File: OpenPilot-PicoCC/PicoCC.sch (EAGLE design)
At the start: 6 parts, among them U1 STM32F103CBT6, X1 MINI-USB-SCHIELD-32005-301

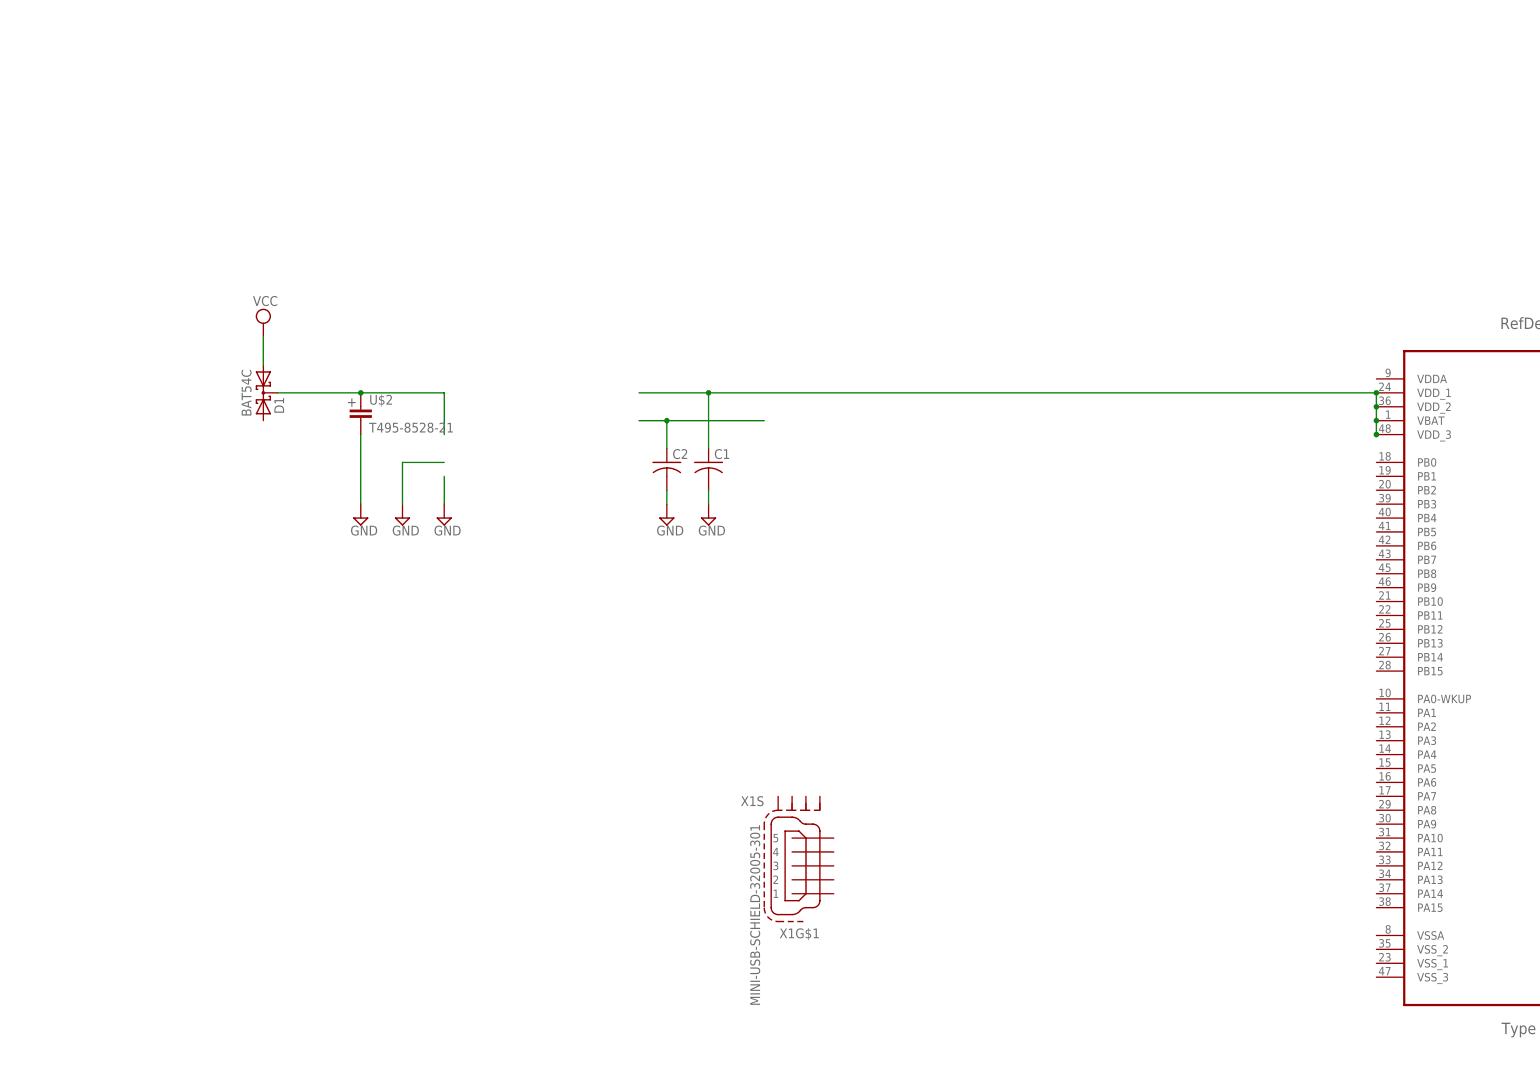
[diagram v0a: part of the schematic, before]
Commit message: Adding a Few things as we go, nice new line protection on the "servo" connectors to prevent shorts.
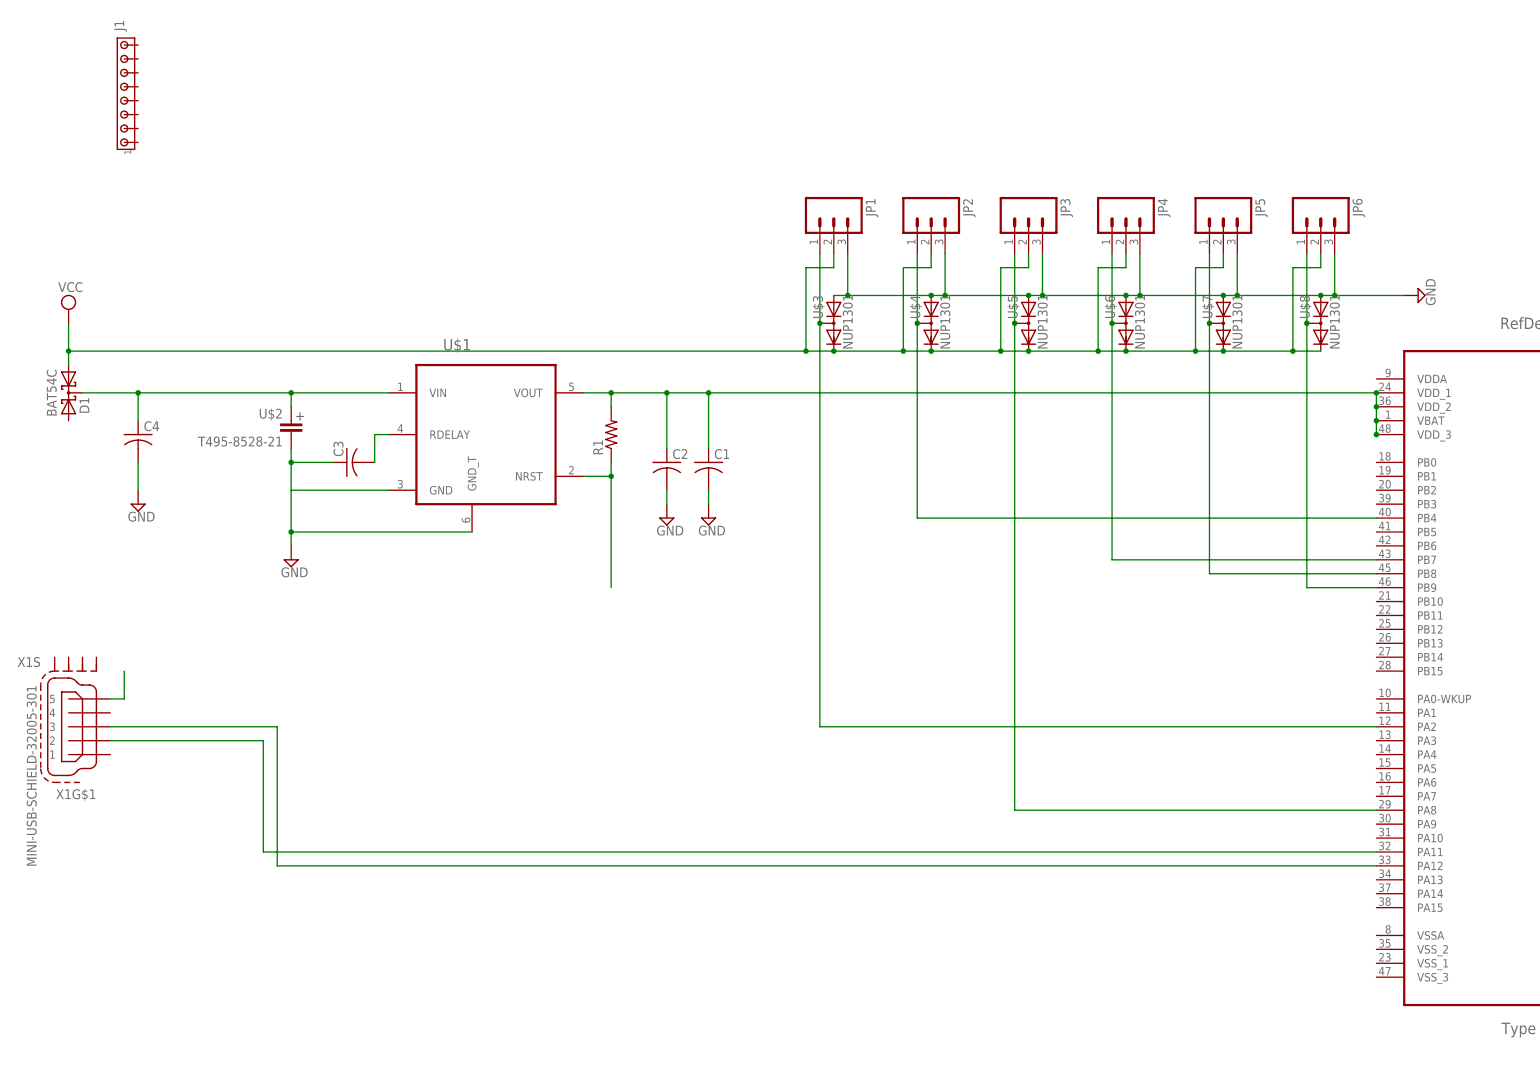
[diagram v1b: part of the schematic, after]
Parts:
- added C3, C4: (no value), rcl:C-USC0402K
- added J1: (no value), con-amp:MTA08-100
- added JP1, JP2, JP3, JP4, JP5, JP6: (no value), SparkFun:M03
- added R1: (no value), rcl:R-US_R0402
- added U$1: (no value), TI_TPS:TPS7A6033-Q1
- added U$3, U$4, U$5, U$6, U$7, U$8: NUP1301, NXP:NUP1301
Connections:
- new net N$10: JP3.1, U$5.3, U1.PA8
- new net N$11: JP4.1, U$6.3, U1.PB7
- new net N$12: JP5.1, U$7.3, U1.PB8
- new net N$13: JP6.1, U$8.3, U1.PB9
- new net N$4: C3.2, U$1.RDELAY
- new net N$5: U1.PA12, X1G$1.3
- new net N$6: R1.1, U$1.NRST
- new net N$7: X1G$1.5
- new net N$8: JP1.1, U$3.3, U1.PA2
- new net N$9: JP2.1, U$4.3, U1.PB4
- net GND: now also C3.1, C4.2, JP1.3, JP2.3, JP3.3, JP4.3, JP5.3, JP6.3, U$1.GND, U$1.GND_T, U$3.1, U$4.1, U$5.1, U$6.1, U$7.1, U$8.1
- net N$1: now also C2.1, R1.2, U$1.VOUT
- net N$2: now also U1.PA11, X1G$1.2; no longer C2.1
- net N$3: now also C4.1, U$1.VIN
- net VCC: now also JP1.2, JP2.2, JP3.2, JP4.2, JP5.2, JP6.2, U$3.2, U$4.2, U$5.2, U$6.2, U$7.2, U$8.2
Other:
- moved on the sheet: D1, U$2, X1G$1, X1S

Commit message: Added the initial HexFET and snubbers. Correct AGND and DGND Seperation. Some Testpoints. Spread Spectrum EMI protection.
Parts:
- added C10, C11, C12, C13, C14, C5, C6, C7, C8, C9: (no value), rcl:C-USC0402K
- added D2, D3, D4, D5, D6, D7: BAS40-05, diode:BAS40-05
- added PAD1, PAD2, PAD3: WIREPADSMD5-2,5, wirepad:WIREPADSMD5-2,5
- added R2, R3, R4: (no value), rcl:R-US_R2512W
- added SJ1: (no value), jumper:SJ2WW
- added TP1, TP10, TP11, TP2, TP3, TP4, TP5, TP6, TP7, TP8, TP9: TPSQTP12R, testpad:TPSQTP12R
- added U$10, U$11, U$12, U$14, U$16, U$18: IRF7309Q, IR-HEXFET:IRF7309Q
- added U$19, U$20, U$21: 2PC4617, NXP:2PC4617
- added U$9: PCS3P258XX, on-semiconductor:PCS3P258XX
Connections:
- removed net GND: C1.2, C2.2, C3.1, C4.2, JP1.3, JP2.3, JP3.3, JP4.3, JP5.3, JP6.3, U$1.GND, U$1.GND_T, U$2.2, U$3.1, U$4.1, U$5.1, U$6.1, U$7.1, U$8.1
- new net AGND: C3.1, C4.2, JP1.3, JP2.3, JP3.3, JP4.3, JP5.3, JP6.3, SJ1.1, TP1.TP, U$1.GND, U$1.GND_T, U$2.2, U$3.1, U$4.1, U$5.1, U$6.1, U$7.1, U$8.1
- new net DGND: C1.2, C2.2, C5.2, C6.2, C7.2, C8.2, SJ1.3, TP2.TP, U$9.FSEL, U$9.S0, U$9.VSS
- new net N$14: TP11.TP, U$9.MODOUT, U1.PD0-OSC_IN
- new net N$15: U$10.N-D$1, U$10.N-D$2, U$10.P-D$1, U$10.P-D$2
- new net N$16: C7.1, C8.1, U$9.VDD
- new net N$17: U$12.N-D$1, U$12.N-D$2, U$12.P-D$1, U$12.P-D$2
- new net N$18: U$11.N-D$1, U$11.N-D$2, U$11.P-D$1, U$11.P-D$2
- new net N$19: U$14.P-G, U$19.P$3
- new net N$20: U$14.N-G
- new net N$21: U$18.N-G
- new net N$22: U$16.P-G, U$20.P$3
- new net N$23: U$16.N-G
- new net N$24: U$18.P-G, U$21.P$3
- new net N$25: C10.2, C9.2, D2.A1, D2.C, D3.A1, R2.1, U$14.N-D$1, U$14.N-D$2, U$14.P-D$1, U$14.P-D$2
- new net N$26: PAD1.P, R2.2
- new net N$27: PAD2.P, R3.1
- new net N$28: PAD3.P, R4.2
- new net N$29: C9.1, D2.A2, U$14.N-S
- new net N$30: C10.1, D3.A2, D3.C, U$14.P-S
- new net N$31: C13.1, D6.A2, U$18.N-S
- new net N$32: C14.1, D7.A2, D7.C, U$18.P-S
- new net N$33: C11.1, D4.A2, U$16.N-S
- new net N$34: C12.1, D5.A2, D5.C, U$16.P-S
- new net N$35: C13.2, C14.2, D6.A1, D6.C, D7.A1, R4.1, U$18.N-D$1, U$18.N-D$2, U$18.P-D$1, U$18.P-D$2
- new net N$36: C11.2, C12.2, D4.A1, D4.C, D5.A1, R3.2, U$16.N-D$1, U$16.N-D$2, U$16.P-D$1, U$16.P-D$2
- net N$1: now also TP4.TP
- net N$10: now also TP7.TP
- net N$11: now also TP8.TP
- net N$12: now also TP9.TP
- net N$13: now also TP10.TP
- net N$3: now also TP3.TP
- net N$8: now also TP5.TP
- net N$9: now also TP6.TP
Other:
- note added: "M"
- note added: "Source"

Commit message: Updated Readme Some initial ESD Setup
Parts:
- removed C10, C11, C12, C13, C14, C9: (no value), rcl:C-USC0402K
- removed D2, D3, D4, D5, D6, D7: BAS40-05, diode:BAS40-05
- removed J1: (no value), con-amp:MTA08-100
- removed JP1, JP2, JP3, JP4, JP5, JP6: (no value), SparkFun:M03
- removed PAD1, PAD2, PAD3: WIREPADSMD5-2,5, wirepad:WIREPADSMD5-2,5
- removed U$19: 2PC4617, NXP:2PC4617
- added C15, C16: (no value), rcl:C-USC0402K
- added C17, C18, C19, C20: (no value), rcl:C-USC0402
- added JP10, JP11, JP12, JP7, JP8, JP9: (no value), SparkFun:M03POGO_PIN_HOLES_ONLY
- added R10, R11, R12, R13, R14, R15, R16, R5, R6, R7, R8, R9: (no value), rcl:R-US_R0402
- added U$13: ABM3B, ABRACON:ABM3B
- added U$15, U$17: NUP1301, NXP:NUP1301
- added U$22: PRTR5V0U2D, NXP:PRTR5V0U2D
- added U3: LM4120AIM5-1.8, national-semiconductor:LM4120AIM5-1.8
- added U4: LT6654AHS6-3.3TRMPBF, linear-technology:LT6654AHS6-3.3TRMPBF
- added U5: L3G4200D, SparkFun:L3G4200D
- added X2: 08FLZ-SM1, con-jst:08FLZ-SM1
- R2, R3, R4: device rcl:R-US_R2512W -> rcl:R-US_R0402
- U$10: value IRF7309Q -> ADXL345; device IR-HEXFET:IRF7309Q -> analog-devices:ADXL345
- U$11: value IRF7309Q -> S2SFL064K; device IR-HEXFET:IRF7309Q -> SPANSION:S2SFL064K
- U$12, U$14, U$16, U$18: value IRF7309Q -> NUP1301; device IR-HEXFET:IRF7309Q -> NXP:NUP1301
- U$20: value 2PC4617 -> PRTR5V0U4D; device NXP:2PC4617 -> NXP:PRTR5V0U4D
- U$21: value 2PC4617 -> PRTR5V0U2D; device NXP:2PC4617 -> NXP:PRTR5V0U2D
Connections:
- removed net N$36: C11.2, C12.2, D4.A1, D4.C, D5.A1, R3.2, U$16.N-D$1, U$16.N-D$2, U$16.P-D$1, U$16.P-D$2
- removed net N$7: X1G$1.5
- new net 3.3V: C1.1, C15.1, C17.1, C18.1, C2.1, C7.1, C8.1, R1.2, R5.2, R6.2, TP4.TP, U$1.VOUT, U$10.RES-VS, U$10.VS, U$11.HOLD_(IO3), U$11.VCC, U$11.WP_(IO2), U$9.VDD, U1.VBAT, U1.VDD_1, U1.VDD_2, U1.VDD_3, U3.EN, U3.VIN, U5.RSVDV@0, U5.VDD, U5.VDDIO
- new net D+: U$22.6, U1.PA11
- new net D-: U$22.4, U1.PA12
- new net N$37: C6.1, U$13.CR2, U$9.XOUT
- new net N$38: C5.1, U$13.CR1, U$9.XIN
- new net N$40: U$10.INT1, U1.PC14-OSC32_IN
- new net N$41: U$10.INT2, U1.PC13-TAMPER-RTC
- new net N$43: R6.1, U$10.!CS, U1.PB12
- new net N$46: C20.1, R7.1
- new net N$47: C19.2, C20.2, U5.PLL
- new net VBUS: U$22.5, X1G$1.1
- new net VEE: C16.1, U3.VOUT
- net AGND: now also JP10.3, JP11.3, JP12.3, JP7.3, JP8.3, JP9.3, U$12.1, U$14.1, U$15.1, U$16.1, U$17.1, U$18.1, U$22.2, X1G$1.5, X1S.S1, X1S.S2, X1S.S3, X1S.S4, X2-1.1; no longer JP1.3, JP2.3, JP3.3, JP4.3, JP5.3, JP6.3
- net DGND: now also C15.2, C16.2, C17.2, C18.2, C19.1, R7.2, U$10.GND2, U$10.GND4, U$10.GND5, U$10.RES-GND, U$11.GND, U$13.GND1, U$13.GND2, U3.GND, U5.GND, U5.RSDVG@3, U5.RSVDG@0, U5.RSVDG@1, U5.RSVDG@2, U5.RSVDG@4
- net N$1: now also R16.2, R2.1, U$12.3; no longer C1.1, C2.1, R1.2, TP4.TP, U$1.VOUT, U1.VBAT, U1.VDD_1, U1.VDD_2, U1.VDD_3
- net N$10: now also JP9.1; no longer JP3.1
- net N$11: now also JP10.1; no longer JP4.1
- net N$12: now also JP11.1; no longer JP5.1
- net N$13: now also JP12.1; no longer JP6.1
- net N$15: now also R5.1, U$11.CS, U1.PA7; no longer U$10.N-D$1, U$10.N-D$2, U$10.P-D$1, U$10.P-D$2
- net N$16: now also U$11.CLK, U1.PB13; no longer C7.1, C8.1, U$9.VDD
- net N$17: now also U$10.SDA, U$11.SI_(IO0), U1.PB15; no longer U$12.N-D$1, U$12.N-D$2, U$12.P-D$1, U$12.P-D$2
- net N$18: now also U$10.SDO, U$11.SO_(IO1), U1.PB14; no longer U$11.N-D$1, U$11.N-D$2, U$11.P-D$1, U$11.P-D$2
- net N$19: now also R2.2, X2-8.1; no longer U$14.P-G, U$19.P$3
- net N$2: now also U$22.1; no longer U1.PA11
- net N$20: now also R15.2, R3.1, U$14.3; no longer U$14.N-G
- net N$21: now also R14.2, R4.1, U$15.3; no longer U$18.N-G
- net N$22: now also R8.2, X2-5.1; no longer U$16.P-G, U$20.P$3
- net N$23: now also R3.2, X2-7.1; no longer U$16.N-G
- net N$24: now also R10.2, X2-3.1; no longer U$18.P-G, U$21.P$3
- net N$25: now also R9.2, X2-4.1; no longer C10.2, C9.2, D2.A1, D2.C, D3.A1, R2.1, U$14.N-D$1, U$14.N-D$2, U$14.P-D$1, U$14.P-D$2
- net N$26: now also R13.2, R8.1, U$16.3; no longer PAD1.P, R2.2
- net N$27: now also R12.2, R9.1, U$17.3; no longer PAD2.P, R3.1
- net N$28: now also R10.1, R11.2, U$18.3; no longer PAD3.P, R4.2
- net N$29: now also R4.2, X2-6.1; no longer C9.1, D2.A2, U$14.N-S
- net N$30: now also R16.1, U1.PA1; no longer C10.1, D3.A2, D3.C, U$14.P-S
- net N$31: now also R15.1, U1.PA0-WKUP; no longer C13.1, D6.A2, U$18.N-S
- net N$32: now also R14.1, U1.PB1; no longer C14.1, D7.A2, D7.C, U$18.P-S
- net N$33: now also R13.1, U1.PB0; no longer C11.1, D4.A2, U$16.N-S
- net N$34: now also R12.1, U1.PB5; no longer C12.1, D5.A2, D5.C, U$16.P-S
- net N$35: now also R11.1, U1.PB6; no longer C13.2, C14.2, D6.A1, D6.C, D7.A1, R4.1, U$18.N-D$1, U$18.N-D$2, U$18.P-D$1, U$18.P-D$2
- net N$5: now also U$22.3; no longer U1.PA12
- net N$8: now also JP7.1; no longer JP1.1
- net N$9: now also JP8.1; no longer JP2.1
- net VCC: now also JP10.2, JP11.2, JP12.2, JP7.2, JP8.2, JP9.2, U$12.2, U$14.2, U$15.2, U$16.2, U$17.2, U$18.2, X2-2.1; no longer JP1.2, JP2.2, JP3.2, JP4.2, JP5.2, JP6.2
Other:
- note removed: "M"
- note removed: "Source"
- moved on the sheet: C5, C6, R2, R3, R4, X1G$1, X1S
